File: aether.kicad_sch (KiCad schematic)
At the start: 49 parts, among them J2 USB_C_Receptacle_USB2.0, Q1 NPN, Q2 NPN, Q3 NPN, Q4 NPN, Q5 NPN, SW1 SW_SPDT, SW3 SW_Push, U13 STM32F405RGTx, U14 STM32F405VGTx, U17 STM32F405RGTx, U4 USBLC6-2SC6, Y1 25MHz

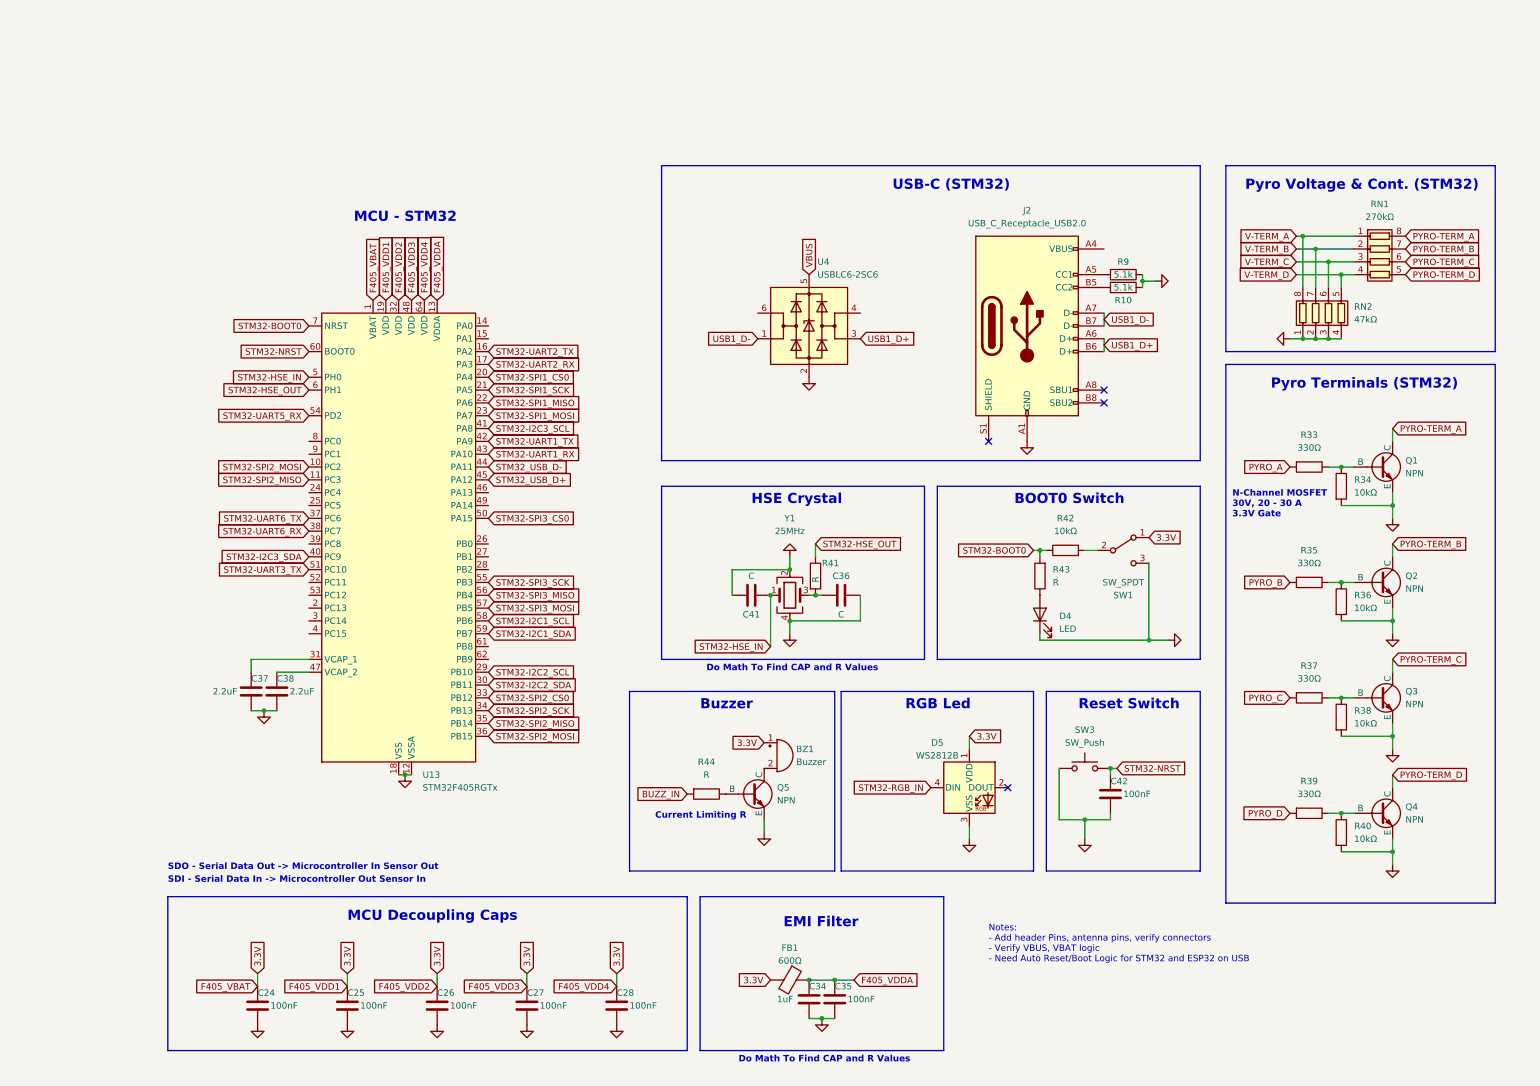
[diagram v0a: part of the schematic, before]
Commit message: Added OSH Logo
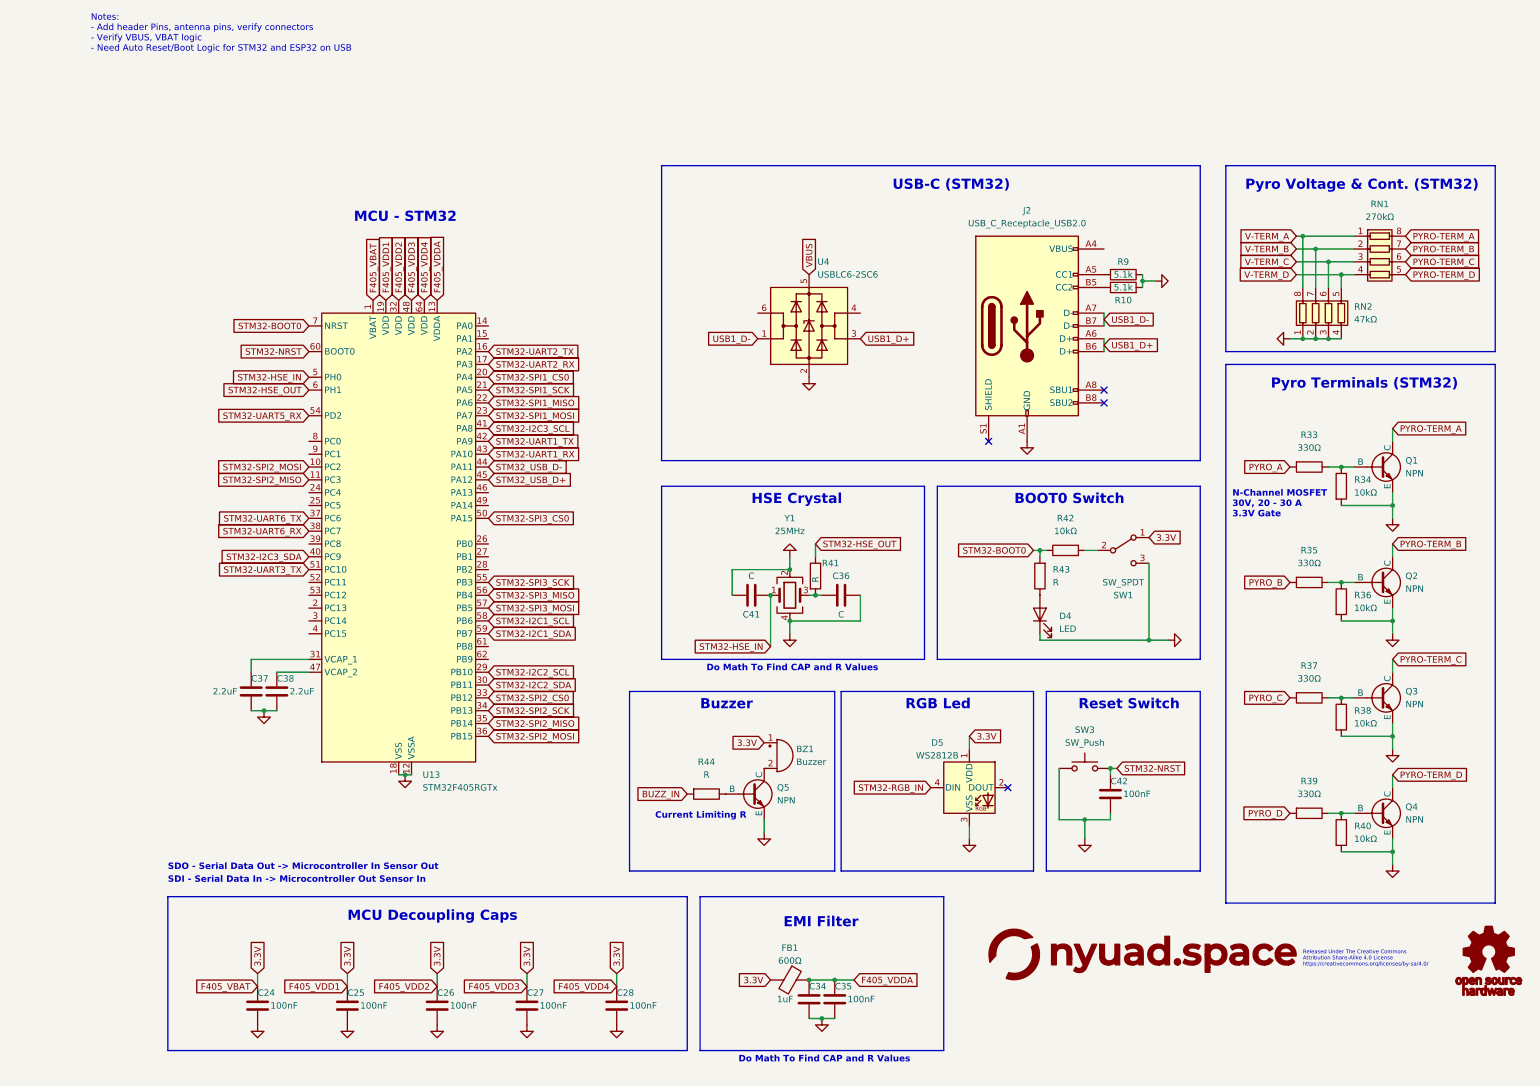
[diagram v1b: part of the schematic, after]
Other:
- note added: "Released Under The Creative Commons Attribution Share-Alike 4.0 License https://creativecommons.orq/licenses/by-sa/4.0/"
- company: nyuad.space -> Aether Flight Computer
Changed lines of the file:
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@@
   (title_block
     (title "MCU - STM32 Schematic")
-    (company "nyuad.space")
-    (comment 1 "Aether Flight Computer")
+    (company "Aether Flight Computer")
+    (comment 7 "Aether Flight Computer")
   )
   (junction (at 35.56 424.18) (diameter 0) (color 0 0 0 0)
@@
     (effects (font (size 1.27 1.27) bold) (justify left bottom))
   )
+  (text "Released Under The Creative Commons\nAttribution Share-Alike 4.0 License\nhttps://creativecommons.orq/licenses/by-sa/4.0/"
+    (at 240.03 175.26 0)
+    (effects (font (face "KiCad Font") (size 0.75 0.75)) (justify left bottom))
+  )
   (text "Notes:\n- Add header Pins, antenna pins, verify connectors\n- Verify VBUS, VBAT logic\n- Need Auto Reset/Boot Logic for STM32 and ESP32 on USB\n\n"
-    (at 177.8 176.53 0)
+    (at 0 -3.81 0)
     (effects (font (size 1.27 1.27)) (justify left bottom))
   )
@@
         (path "/e12346fa-509d-4de9-8ab1-dced307292db"
           (reference "#PWR067") (unit 1)
+        )
+      )
+    )
+  )
+  (symbol (lib_id "osh_logo:LOGO") (at 276.86 173.99 0) (unit 1)
+    (in_bom yes) (on_board yes) (dnp no) (fields_autoplaced)
+    (property "Reference" "#G1" (at 276.86 167.7874 0)
+      (effects (font (size 1.27 1.27)) hide)
+    )
+    (property "Value" "LOGO" (at 276.86 180.1926 0)
+      (effects (font (size 1.27 1.27)) hide)
+    )
+    (property "Footprint" "" (at 276.86 173.99 0)
+      (effects (font (size 1.27 1.27)) hide)
+    )
+    (property "Datasheet" "" (at 276.86 173.99 0)
+      (effects (font (size 1.27 1.27)) hide)
+    )
+    (instances
+      (project "aether"
+        (path "/e12346fa-509d-4de9-8ab1-dced307292db"
+          (reference "#G1") (unit 1)
         )
       )
@@
         )
       )
+    )
+  )
+  (symbol (lib_id "nyuad_space:LOGO") (at 208.28 172.72 0) (unit 1)
+    (in_bom yes) (on_board yes) (dnp no) (fields_autoplaced)
+    (property "Reference" "#G2" (at 208.28 168.3609 0)
+      (effects (font (size 1.27 1.27)) hide)
+    )
+    (property "Value" "LOGO" (at 208.28 177.0791 0)
+      (effects (font (size 1.27 1.27)) hide)
+    )
+    (property "Footprint" "" (at 208.28 172.72 0)
+      (effects (font (size 1.27 1.27)) hide)
+    )
+    (property "Datasheet" "" (at 208.28 172.72 0)
+      (effects (font (size 1.27 1.27)) hide)
+    )
+    (instances
+      (project "aether"
+        (path "/e12346fa-509d-4de9-8ab1-dced307292db"
+          (reference "#G2") (unit 1)
+        )
+      )

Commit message: Updated files
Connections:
- net STM32-UART3_RX: now also U13.52 (PC11)
- net STM32-UART5_RX: no longer U13.54 (PD2)
- net STM32-UART6_RX: no longer U13.38 (PC7)
- net STM32-UART6_TX: no longer U13.37 (PC6)
- net V-TERM_A: now also U13.8 (PC0)
- net V-TERM_B: now also U13.9 (PC1)
- net V-TERM_C: now also U13.10 (PC2)
- net V-TERM_D: now also U13.11 (PC3)
- net DPS310_CSB renamed STM32-SPI2_CS0
- net DPS310_SCK renamed STM32-SPI2_SCK
- net DPS310_SDI/SDA renamed STM32-SPI2_MISO
- net STM32-SPI2_MISO: no longer U13.11 (PC3)
- net DPS310_SDO renamed STM32-SPI2_MOSI
- net STM32-SPI2_MOSI: no longer U13.10 (PC2)
- net FLASH_CLK renamed STM32-SPI1_SCK
- net FLASH_CS renamed STM32-SPI1_CS0
- net FLASH_SDI renamed STM32-SPI1_MISO
- net FLASH_SDO renamed STM32-SPI1_MOSI
- net GPS_SCL renamed STM32-I2C1_SCL
- net GPS_SDA renamed STM32-I2C1_SDA
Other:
- note added: "I2C1"
- note added: "I2C2"
- note added: "SPI1"
- note added: "SPI2"
- note added: "SPI3"
- note added: "UART1"
- note added: "UART2"
- note removed: "0x40, 0x76"
- note removed: "0x41"
- note removed: "0x42"
- note removed: "0x44"
- note removed: "I2C 1 (STM32)"
- note removed: "Released Under The Creative Commons Attribution Share-Alike 4.0 License https://creativecommons.orq/licenses/by-sa/4.0/"
- note removed: "SPI 1 (ESP32)"
- note removed: "SPI 1 (STM32)"
- note removed: "SPI 2 (STM32)"

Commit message: Added INA219
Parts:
- removed C32, C33, C39, C40: 2.2uF, Capacitor_SMD:C_0201_0603Metric, symbol Device:C
- removed R34, R36, R38, R40: 10kΩ, symbol Device:R
- removed U14: STM32F405VGTx, Package_QFP:LQFP-100_14x14mm_P0.5mm, symbol MCU_ST_STM32F4:STM32F405VGTx
- removed U17: STM32F405RGTx, Package_QFP:LQFP-64_10x10mm_P0.5mm, symbol MCU_ST_STM32F4:STM32F405RGTx
- added RN4: 10kΩ, symbol Device:R_Pack04
- C36, C41: value C -> 10pF
- R41: value R -> 620
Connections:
- net GND: now also RN4.5 (R4.2), RN4.6 (R3.2), RN4.7 (R2.2), RN4.8 (R1.2)
- net STM32-BOOT0: now also U13.60 (BOOT0); no longer U13.7 (NRST)
- net STM32-NRST: now also U13.7 (NRST); no longer U13.60 (BOOT0)
- net STM32-SPI2_CS1: now also U13.25 (PC5)
- net STM32-SPI2_CS2: now also U13.37 (PC6)
- net STM32-SPI2_CS3: now also U13.38 (PC7)
- net STM32_USB_D+: now also U4.4 (I/O2)
- net STM32_USB_D-: now also U4.6 (I/O1)
- net at Q4.2 (B), R39.1: now also RN4.1 (R1.1)
- net at Q1.2 (B), R33.1: now also RN4.4 (R4.1)
- net at Q3.2 (B), R37.1: now also RN4.2 (R2.1)
- net at Q2.2 (B), R35.1: now also RN4.3 (R3.1)
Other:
- note added: "ABM8G-25.000MHZ-4Y-T3"
- note added: "BOOT0"
- note added: "C = 2 * (CL - Cstray) Cstray = {2pF, 5pf} Rext = 1/(2*pi*f*CL2)"
- note added: "Do BOOT0 & RST Pins have internal pull-ups/pull-downs?"
- note added: "I2C3"
- note added: "NRST"
- note added: "Replace with 'Mini'"
- note added: "UART3"
- note added: "USB"
- note removed: "MCU - STM32 (F405)"
- moved on the sheet: C36, C37, C38, C41, Q1, Q2, Q3, Q4, R33, R35, R37, R39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

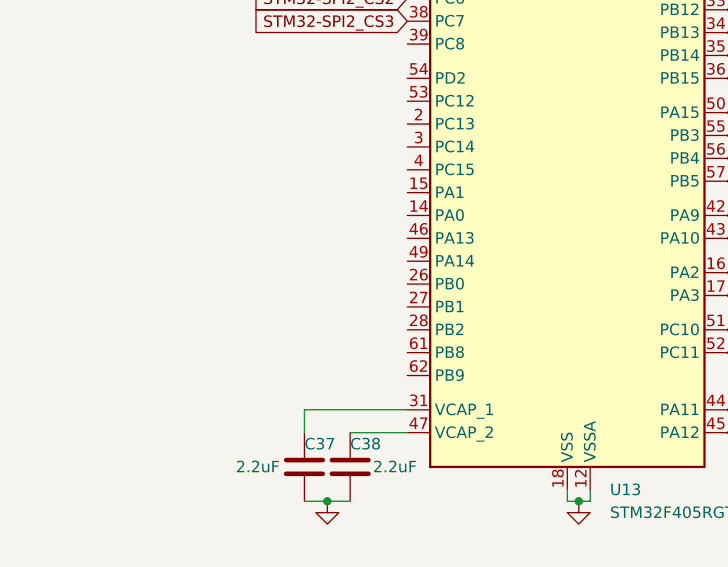
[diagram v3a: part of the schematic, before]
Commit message: Added connectors
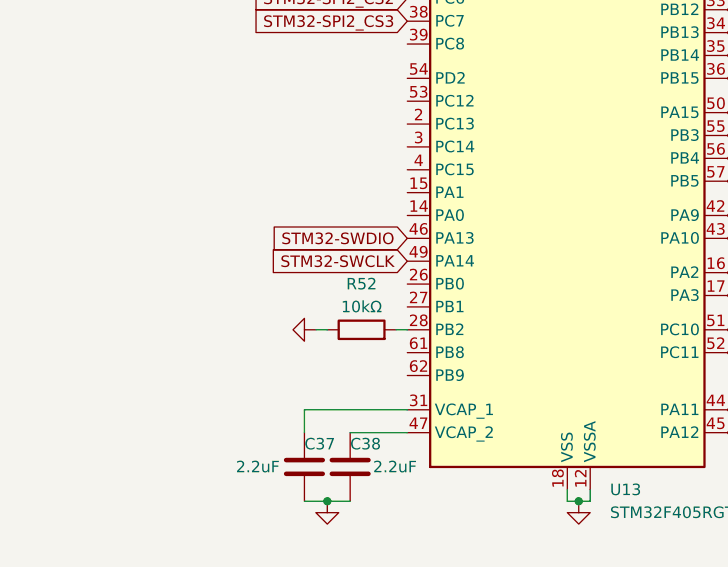
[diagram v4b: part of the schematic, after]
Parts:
- added R52: 10kΩ, symbol Device:R
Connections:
- net GND: now also R52.1
- net at U13.28 (PB2): now also R52.2
- net STM32-SWDIO: now reaches U13.46 (PA13)
- net STM32-SWCLK: now reaches U13.49 (PA14)
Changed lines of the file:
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@@
+    (stroke (width 0) (type default))
+  )
+  (wire (pts (xy 41.91 119.38) (xy 43.18 119.38))
     (stroke (width 0) (type default))
   )
@@
   )
   (wire (pts (xy 187.96 92.71) (xy 189.23 92.71))
+    (stroke (width 0) (type default))
+  )
+  (wire (pts (xy 34.29 119.38) (xy 33.02 119.38))
     (stroke (width 0) (type default))
   )
@@
     )
   )
+  (global_label "STM32-SWDIO" (shape input) (at 43.18 109.22 180) (fields_autoplaced)
+    (effects (font (size 1.27 1.27)) (justify right))
+    (property "Intersheetrefs" "${INTERSHEET_REFS}" (at 26.7087 109.22 0)
+      (effects (font (size 1.27 1.27)) (justify right) hide)
+    )
+  )
   (global_label "STM32-SPI2_SCK" (shape input) (at 78.74 86.36 0) (fields_autoplaced)
     (effects (font (size 1.27 1.27)) (justify left))
@@
     (property "Intersheetrefs" "${INTERSHEET_REFS}" (at 50.8 169.4324 90)
       (effects (font (size 1.27 1.27)) (justify left) hide)
+    )
+  )
+  (global_label "STM32-SWCLK" (shape input) (at 43.18 111.76 180) (fields_autoplaced)
+    (effects (font (size 1.27 1.27)) (justify right))
+    (property "Intersheetrefs" "${INTERSHEET_REFS}" (at 26.3459 111.76 0)
+      (effects (font (size 1.27 1.27)) (justify right) hide)
     )
   )
@@
         )
       )
+    )
+  )
+  (symbol (lib_id "Device:R") (at 38.1 119.38 90) (unit 1)
+    (in_bom yes) (on_board yes) (dnp no)
+    (property "Reference" "R52" (at 38.1 114.3 90)
+      (effects (font (size 1.27 1.27)))
+    )
+    (property "Value" "10kΩ" (at 38.1 116.84 90)
+      (effects (font (size 1.27 1.27)))
+    )
+    (property "Footprint" "" (at 38.1 121.158 90)
+      (effects (font (size 1.27 1.27)) hide)
+    )
+    (property "Datasheet" "~" (at 38.1 119.38 0)
+      (effects (font (size 1.27 1.27)) hide)
+    )
+    (pin "1")
+    (pin "2")
+    (instances
+      (project "aether"
+        (path "/e12346fa-509d-4de9-8ab1-dced307292db"
+          (reference "R52") (unit 1)
+        )
+      )
+    )
+  )
+  (symbol (lib_id "power:GND") (at 33.02 119.38 270) (unit 1)
+    (in_bom yes) (on_board yes) (dnp no) (fields_autoplaced)
+    (property "Reference" "#PWR066" (at 26.67 119.38 0)
+      (effects (font (size 1.27 1.27)) hide)
+    )
+    (property "Value" "GND" (at 29.21 119.38 90)
+      (effects (font (size 1.27 1.27)) (justify right) hide)
+    )
+    (property "Footprint" "" (at 33.02 119.38 0)
+      (effects (font (size 1.27 1.27)) hide)
+    )
+    (property "Datasheet" "" (at 33.02 119.38 0)
+      (effects (font (size 1.27 1.27)) hide)
+    )
+    (pin "1")
+    (instances
+      (project "aether"
+        (path "/e12346fa-509d-4de9-8ab1-dced307292db"
+          (reference "#PWR066") (unit 1)
+        )
+      )
